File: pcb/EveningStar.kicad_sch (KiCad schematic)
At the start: 4 parts

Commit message: sch: move usb to separate sheet
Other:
- added sheet usb (usb.kicad_sch)
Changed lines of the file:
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@@
+	)
+	(sheet
+		(at 99.06 113.03)
+		(size 29.21 5.08)
+		(exclude_from_sim no)
+		(in_bom yes)
+		(on_board yes)
+		(dnp no)
+		(fields_autoplaced yes)
+		(stroke
+			(width 0.1524)
+			(type solid)
+		)
+		(fill
+			(color 0 0 0 0)
+		)
+		(property "Sheetname" "usb"
+			(at 99.06 112.3184 0)
+			(show_name no)
+			(do_not_autoplace no)
+			(effects
+				(font
+					(size 1.27 1.27)
+				)
+				(justify left bottom)
+			)
+		)
+		(property "Sheetfile" "usb.kicad_sch"
+			(at 99.06 118.6946 0)
+			(show_name no)
+			(do_not_autoplace no)
+			(effects
+				(font
+					(size 1.27 1.27)
+				)
+				(justify left top)
+			)
+		)
+		(pin "{USB}" input
+			(at 99.06 115.57 180)
+			(effects
+				(font
+					(size 1.27 1.27)
+				)
+				(justify left)
+			)
+		)
+		(instances
+			(project "EveningStar"
+				(path "/4c61f5a2-f8d4-462a-9bc3-d74437d30372"
+					(page "7")
+				)
+			)
+		)
 	)
 	(sheet

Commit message: sch: replace mcu and clean up schematic
Fixes #27
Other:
- sheet mcu ports: added ETH_CS, ETH_INT, ETH_RST, {I2C}, {METERBUS_IO}, {SPI}, {USB}; removed none
- sheet meterbus_frontend ports: added {METERBUS_IO}; removed none
- note added: "JLC assembly mounts"
- moved on the sheet: H1, H2, H3, H4

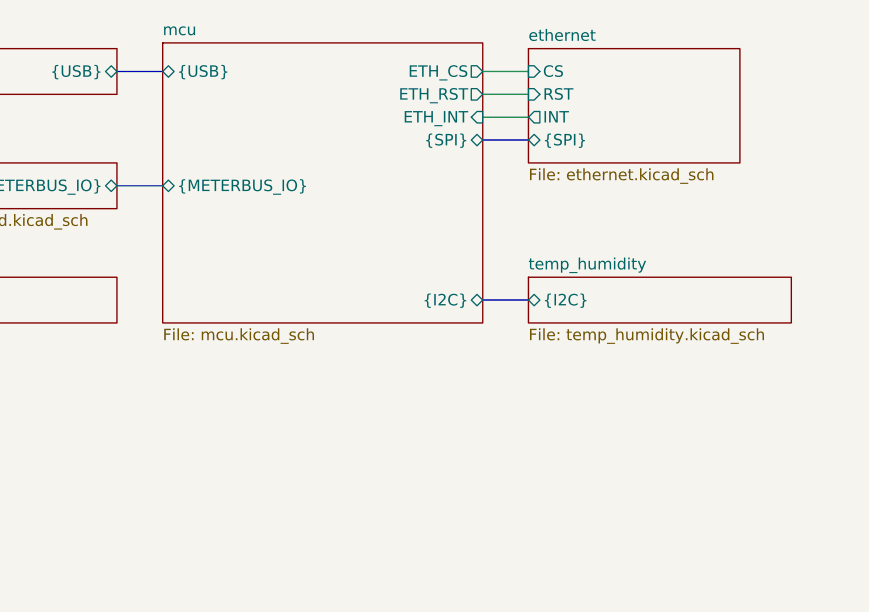
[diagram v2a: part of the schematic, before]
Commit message: sch: add flash ic
Fixes #11
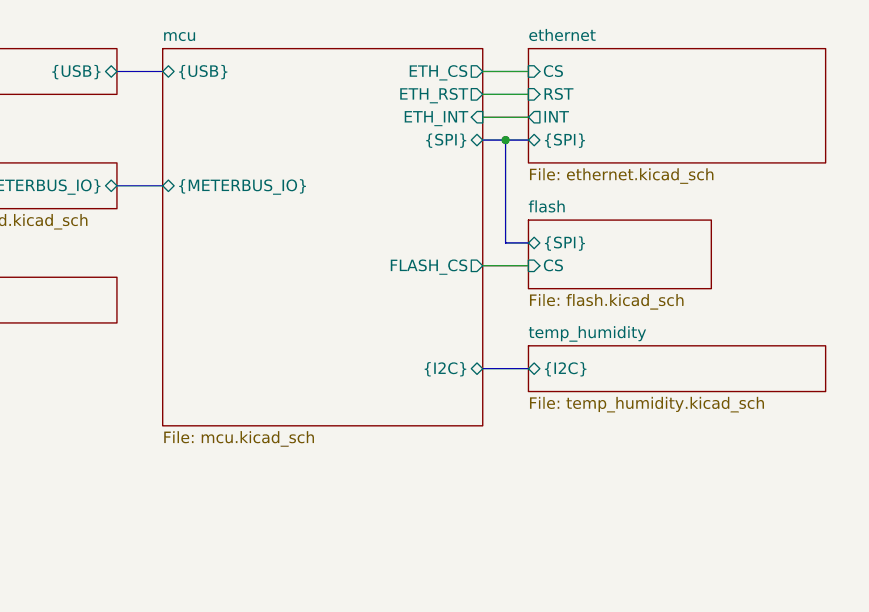
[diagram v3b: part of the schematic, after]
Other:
- added sheet flash (flash.kicad_sch)
- sheet mcu ports: added FLASH_CS; removed none
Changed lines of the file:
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@@
 		)
+	)
+	(junction
+		(at 97.79 30.48)
+		(diameter 0)
+		(color 0 0 0 0)
 	)
 	(bus
 		(pts
-			(xy 95.25 48.26) (xy 100.33 48.26)
+			(xy 95.25 55.88) (xy 100.33 55.88)
+		)
+		(stroke
+			(width 0)
+			(type default)
+		)
+	)
+	(bus
+		(pts
+			(xy 97.79 30.48) (xy 100.33 30.48)
 		)
 		(stroke
@@
 		)
 	)
+	(bus
+		(pts
+			(xy 97.79 30.48) (xy 97.79 41.91)
+		)
+		(stroke
+			(width 0)
+			(type default)
+		)
+	)
 	(wire
 		(pts
@@
 		)
 	)
+	(bus
+		(pts
+			(xy 97.79 41.91) (xy 100.33 41.91)
+		)
+		(stroke
+			(width 0)
+			(type default)
+		)
+	)
 	(wire
 		(pts
@@
 	(bus
 		(pts
-			(xy 95.25 30.48) (xy 100.33 30.48)
+			(xy 95.25 30.48) (xy 97.79 30.48)
+		)
+		(stroke
+			(width 0)
+			(type default)
+		)
+	)
+	(wire
+		(pts
+			(xy 95.25 44.45) (xy 100.33 44.45)
 		)
 		(stroke
@@
 	)
 	(sheet
-		(at 100.33 20.32)
-		(size 23.495 12.7)
+		(at 100.33 39.37)
+		(size 20.32 7.62)
 		(exclude_from_sim no)
 		(in_bom yes)
@@
 			(color 0 0 0 0)
 		)
+		(property "Sheetname" "flash"
+			(at 100.33 38.6584 0)
+			(show_name no)
+			(do_not_autoplace no)
+			(effects
+				(font
+					(size 1.27 1.27)
+				)
+				(justify left bottom)
+			)
+		)
+		(property "Sheetfile" "flash.kicad_sch"
+			(at 100.33 47.5746 0)
+			(show_name no)
+			(do_not_autoplace no)
+			(effects
+				(font
+					(size 1.27 1.27)
+				)
+				(justify left top)
+			)
+		)
+		(pin "{SPI}" bidirectional
+			(at 100.33 41.91 180)
+			(effects
+				(font
+					(size 1.27 1.27)
+				)
+				(justify left)
+			)
+		)
+		(pin "CS" input
+			(at 100.33 44.45 180)
+			(effects
+				(font
+					(size 1.27 1.27)
+				)
+				(justify left)
+			)
+		)
+		(instances
+			(project "EveningStar"
+				(path "/4c61f5a2-f8d4-462a-9bc3-d74437d30372"
+					(page "8")
+				)
+			)
+		)
+	)
+	(sheet
+		(at 100.33 20.32)
+		(size 33.02 12.7)
+		(exclude_from_sim no)
+		(in_bom yes)
+		(on_board yes)
+		(dnp no)
+		(fields_autoplaced yes)
+		(stroke
+			(width 0.1524)
+			(type solid)
+		)
+		(fill
+			(color 0 0 0 0)
+		)
 		(property "Sheetname" "ethernet"
 			(at 100.33 19.6084 0)
@@
 	)
 	(sheet
-		(at 100.33 45.72)
-		(size 29.21 5.08)
+		(at 100.33 53.34)
+		(size 33.02 5.08)
 		(exclude_from_sim no)
 		(in_bom yes)
@@
 		)
 		(property "Sheetname" "temp_humidity"
-			(at 100.33 45.0084 0)
+			(at 100.33 52.6284 0)
 			(show_name no)
 			(do_not_autoplace no)
@@
 		)
 		(property "Sheetfile" "temp_humidity.kicad_sch"
-			(at 100.33 51.3846 0)
+			(at 100.33 59.0046 0)
 			(show_name no)
 			(do_not_autoplace no)
@@
 		)
 		(pin "{I2C}" bidirectional
-			(at 100.33 48.26 180)
+			(at 100.33 55.88 180)
 			(effects
 				(font
@@
 	)
 	(sheet
-		(at 59.69 19.685)
-		(size 35.56 31.115)
+		(at 59.69 20.32)
+		(size 35.56 41.91)
 		(exclude_from_sim no)
 		(in_bom yes)
@@
 		)
 		(property "Sheetname" "mcu"
-			(at 59.69 18.9734 0)
+			(at 59.69 19.6084 0)
 			(show_name no)
 			(do_not_autoplace no)
@@
 		)
 		(property "Sheetfile" "mcu.kicad_sch"
-			(at 59.69 51.3846 0)
+			(at 59.69 62.8146 0)
 			(show_name no)
 			(do_not_autoplace no)
@@
 		)
 		(pin "{I2C}" bidirectional
-			(at 95.25 48.26 0)
+			(at 95.25 55.88 0)
 			(effects
 				(font
@@
 			(effects
 				(font
+					(size 1.27 1.27)
+				)
+				(justify right)
+			)
+		)
+		(pin "FLASH_CS" output
+			(at 95.25 44.45 0)
+			(effects
+				(font

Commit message: sch: add 32khz rtc crystal
Fixes #21
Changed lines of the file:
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@@
 	(sheet
 		(at 59.69 20.32)
-		(size 35.56 41.91)
+		(size 35.56 38.1)
 		(exclude_from_sim no)
 		(in_bom yes)
@@
 		)
 		(property "Sheetfile" "mcu.kicad_sch"
-			(at 59.69 62.8146 0)
+			(at 59.69 59.0046 0)
 			(show_name no)
 			(do_not_autoplace no)

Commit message: sch: remove aht20 temp humidity sensor
Fixes #49
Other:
- removed sheet temp_humidity
- sheet mcu ports: added none; removed {I2C}
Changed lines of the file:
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@@
-	(bus
-		(pts
-			(xy 95.25 55.88) (xy 100.33 55.88)
-		)
-		(stroke
-			(width 0)
-			(type default)
-		)
-	)
 	(bus
 		(pts
@@
 	)
 	(sheet
-		(at 100.33 53.34)
-		(size 33.02 5.08)
+		(at 59.69 20.32)
+		(size 35.56 38.1)
 		(exclude_from_sim no)
 		(in_bom yes)
@@
 			(color 0 0 0 0)
 		)
-		(property "Sheetname" "temp_humidity"
-			(at 100.33 52.6284 0)
-			(show_name no)
-			(do_not_autoplace no)
-			(effects
-				(font
-					(size 1.27 1.27)
-				)
-				(justify left bottom)
-			)
-		)
-		(property "Sheetfile" "temp_humidity.kicad_sch"
-			(at 100.33 59.0046 0)
-			(show_name no)
-			(do_not_autoplace no)
-			(effects
-				(font
-					(size 1.27 1.27)
-				)
-				(justify left top)
-			)
-		)
-		(pin "{I2C}" bidirectional
-			(at 100.33 55.88 180)
-			(effects
-				(font
-					(size 1.27 1.27)
-				)
-				(justify left)
-			)
-		)
-		(instances
-			(project "EveningStar"
-				(path "/4c61f5a2-f8d4-462a-9bc3-d74437d30372"
-					(page "6")
-				)
-			)
-		)
-	)
-	(sheet
-		(at 59.69 20.32)
-		(size 35.56 38.1)
-		(exclude_from_sim no)
-		(in_bom yes)
-		(on_board yes)
-		(dnp no)
-		(fields_autoplaced yes)
-		(stroke
-			(width 0.1524)
-			(type solid)
-		)
-		(fill
-			(color 0 0 0 0)
-		)
 		(property "Sheetname" "mcu"
 			(at 59.69 19.6084 0)
@@
 			(effects
 				(font
-					(size 1.27 1.27)
-				)
-				(justify right)
-			)
-		)
-		(pin "{I2C}" bidirectional
-			(at 95.25 55.88 0)
-			(effects
-				(font

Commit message: sch: reset esp32 using dc-dc pgood line
This avoids the needs for a voltage supervisor, and provides some protection against brownouts and glitches
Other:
- sheet mcu ports: added PGOOD; removed none
- sheet psu ports: added PGOOD; removed none
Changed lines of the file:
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@@
+	(wire
+		(pts
+			(xy 54.61 48.26) (xy 59.69 48.26)
+		)
+		(stroke
+			(width 0)
+			(type default)
+		)
+	)
 	(wire
 		(pts
@@
 			)
 		)
+		(pin "PGOOD" output
+			(at 54.61 48.26 0)
+			(effects
+				(font
+					(size 1.27 1.27)
+				)
+				(justify right)
+			)
+		)
 		(instances
 			(project "EveningStar"
@@
 			)
 		)
+		(pin "PGOOD" input
+			(at 59.69 48.26 180)
+			(effects
+				(font
+					(size 1.27 1.27)
+				)
+				(justify left)
+			)
+		)

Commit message: sch: add schematic titles and do some cleanup
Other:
- company: (none) -> CIA Assured
- title: (none) -> EveningStar
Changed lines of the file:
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@@
 	(generator_version "10.0")
 	(paper "A4")
+	(title_block
+		(title "EveningStar")
+		(company "CIA Assured")
+	)
 	(rectangle
 		(start 17.78 173.99)

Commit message: sch: rewire SPI to supply separate clock lines to flash and ethernet
The flash IC datasheet specifies that the SPI clock must not be toggled
while CS is high, which means we need to separate the ethernet and flash
clock lines.

I've GPIO3 on the ESP for the flash clock line, and plan to use the
internal peripheral MUX to switch it when talking with the IC.

I've also moved a bunch of test points and termination resistors in this
process.
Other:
- sheet ethernet ports: added none; removed CS
- sheet flash ports: added none; removed CS
- sheet mcu ports: added ETH{SPI}, FLASH{SPI}; removed ETH_CS, FLASH_CS, {SPI}
